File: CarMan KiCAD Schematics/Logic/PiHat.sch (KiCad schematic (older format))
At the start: 15 parts

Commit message: Refactored repo
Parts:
- gave numbers to parts that had none: 15
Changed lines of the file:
@@
 5V
 $Comp
-L Interface_CAN_LIN:MCP2515-xSO U?
+L Interface_CAN_LIN:MCP2515-xSO U8
 U 1 1 5F9A99EE
 P 6750 3100
-F 0 "U?" H 6500 3850 50  0000 C CNN
+F 0 "U8" H 6500 3850 50  0000 C CNN
 F 1 "MCP2515-xSO" H 7200 3850 50  0000 C CNN
 F 2 "Package_SO:SOIC-18W_7.5x11.6mm_P1.27mm" H 6750 2200 50  0001 C CIN
@@
 5V_rtn
 $Comp
-L Connector:Conn_01x02_Male J?
+L Connector:Conn_01x02_Male J7
 U 1 1 5F9AE3B8
 P 2500 1700
-F 0 "J?" V 2562 1744 50  0000 L CNN
+F 0 "J7" V 2562 1744 50  0000 L CNN
 F 1 "Conn_01x02_Male" V 2653 1744 50  0000 L CNN
 F 2 "" H 2500 1700 50  0001 C CNN
@@
 $EndComp
 $Comp
-L Device:R R?
+L Device:R R7
 U 1 1 5F9AF7D2
 P 2500 2050
-F 0 "R?" H 2570 2096 50  0000 L CNN
+F 0 "R7" H 2570 2096 50  0000 L CNN
 F 1 "120" V 2500 2000 50  0000 L CNN
 F 2 "" V 2430 2050 50  0001 C CNN
@@
 	3600 1850 3900 1850
 $Comp
-L Device:C C?
+L Device:C C14
 U 1 1 5F9B08F3
 P 3900 2000
-F 0 "C?" H 4015 2046 50  0000 L CNN
+F 0 "C14" H 4015 2046 50  0000 L CNN
 F 1 "0.1uF" H 4015 1955 50  0000 L CNN
 F 2 "" H 3938 1850 50  0001 C CNN
@@
 	3600 3250 3700 3250
 $Comp
-L Device:R R?
+L Device:R R6
 U 1 1 5F9B1617
 P 2450 3200
-F 0 "R?" H 2520 3246 50  0000 L CNN
+F 0 "R6" H 2520 3246 50  0000 L CNN
 F 1 "100" V 2450 3150 50  0000 L CNN
 F 2 "" V 2380 3200 50  0001 C CNN
@@
 $EndComp
 $Comp
-L Device:C C?
+L Device:C C12
 U 1 1 5F9B20E3
 P 2450 3500
-F 0 "C?" H 2250 3550 50  0000 L CNN
+F 0 "C12" H 2250 3550 50  0000 L CNN
 F 1 "560pF" H 2100 3450 50  0000 L CNN
 F 2 "" H 2488 3350 50  0001 C CNN
@@
 $EndComp
 $Comp
-L Device:R R?
+L Device:R R8
 U 1 1 5F9B2DC0
 P 2750 3200
-F 0 "R?" H 2820 3246 50  0000 L CNN
+F 0 "R8" H 2820 3246 50  0000 L CNN
 F 1 "100" V 2750 3150 50  0000 L CNN
 F 2 "" V 2680 3200 50  0001 C CNN
@@
 $EndComp
 $Comp
-L Device:C C?
+L Device:C C13
 U 1 1 5F9B3945
 P 2750 3500
-F 0 "C?" H 2865 3546 50  0000 L CNN
+F 0 "C13" H 2865 3546 50  0000 L CNN
 F 1 "560pF" H 2865 3455 50  0000 L CNN
 F 2 "" H 2788 3350 50  0001 C CNN
@@
 	4250 2900 4250 3100
 $Comp
-L Device:R R?
+L Device:R R9
 U 1 1 5F9B562B
 P 4250 3250
-F 0 "R?" H 4320 3296 50  0000 L CNN
+F 0 "R9" H 4320 3296 50  0000 L CNN
 F 1 "4k7" V 4250 3200 50  0000 L CNN
 F 2 "" V 4180 3250 50  0001 C CNN
@@
 NoConn ~ 7350 3500
 $Comp
-L Interface_CAN_LIN:MCP2551-I-P U?
+L Interface_CAN_LIN:MCP2551-I-P U7
 U 1 1 5F9A8A6F
 P 3600 2700
-F 0 "U?" H 3300 3050 50  0000 C CNN
+F 0 "U7" H 3300 3050 50  0000 C CNN
 F 1 "MCP2551-I-P" H 4000 3050 50  0000 C CNN
 F 2 "Package_DIP:DIP-8_W7.62mm" H 3600 2200 50  0001 C CIN
@@
 	6750 1850 7050 1850
 $Comp
-L Device:C C?
+L Device:C C15
 U 1 1 5F9BD77C
 P 7050 2000
-F 0 "C?" H 7165 2046 50  0000 L CNN
+F 0 "C15" H 7165 2046 50  0000 L CNN
 F 1 "0.1uF" H 7165 1955 50  0000 L CNN
 F 2 "" H 7088 1850 50  0001 C CNN
@@
 NoConn ~ 6150 3600
 $Comp
-L Device:R R?
+L Device:R R10
 U 1 1 5F9C01C9
 P 5750 3700
-F 0 "R?" V 5850 3700 50  0000 C CNN
+F 0 "R10" V 5850 3700 50  0000 C CNN
 F 1 "4k7" V 5750 3700 50  0000 C CNN
 F 2 "" V 5680 3700 50  0001 C CNN
@@
 PI_SPI_SCLK
 $Comp
-L Device:Crystal Y?
+L Device:Crystal Y1
 U 1 1 5F9C41DC
 P 8150 3350
-F 0 "Y?" V 8104 3481 50  0000 L CNN
+F 0 "Y1" V 8104 3481 50  0000 L CNN
 F 1 "16MHz" V 8195 3481 50  0000 L CNN
 F 2 "" H 8150 3350 50  0001 C CNN
@@
 	7700 3500 8150 3500
 $Comp
-L Device:C C?
+L Device:C C16
 U 1 1 5F9C8133
 P 8750 3200
-F 0 "C?" V 8498 3200 50  0000 C CNN
+F 0 "C16" V 8498 3200 50  0000 C CNN
 F 1 "22pF" V 8589 3200 50  0000 C CNN
 F 2 "" H 8788 3050 50  0001 C CNN
@@
 Connection ~ 8150 3200
 $Comp
-L Device:C C?
+L Device:C C17
 U 1 1 5F9CA3A5
 P 8750 3500
-F 0 "C?" V 9000 3500 50  0000 C CNN
+F 0 "C17" V 9000 3500 50  0000 C CNN
 F 1 "22pF" V 8900 3500 50  0000 C CNN
 F 2 "" H 8788 3350 50  0001 C CNN

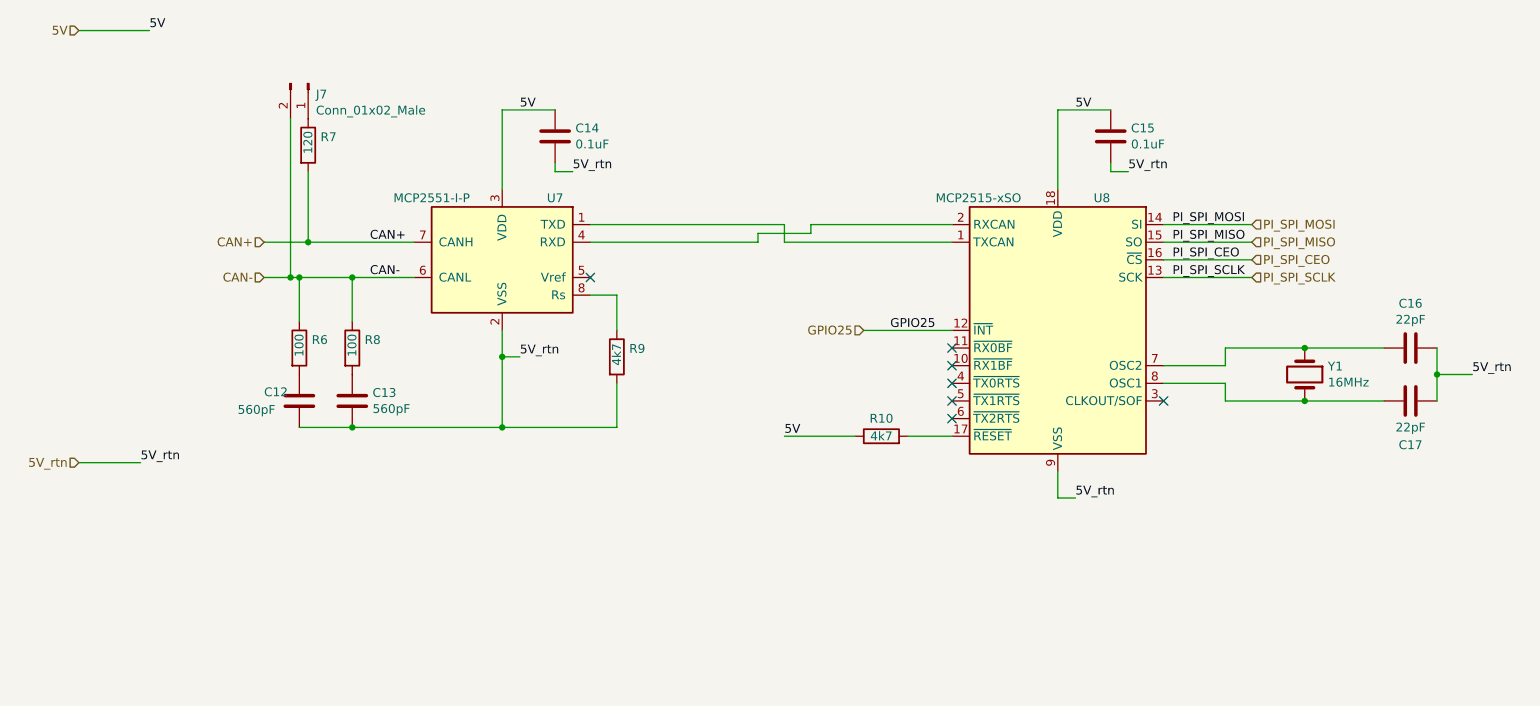
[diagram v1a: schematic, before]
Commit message: Added isolation to CANBUS
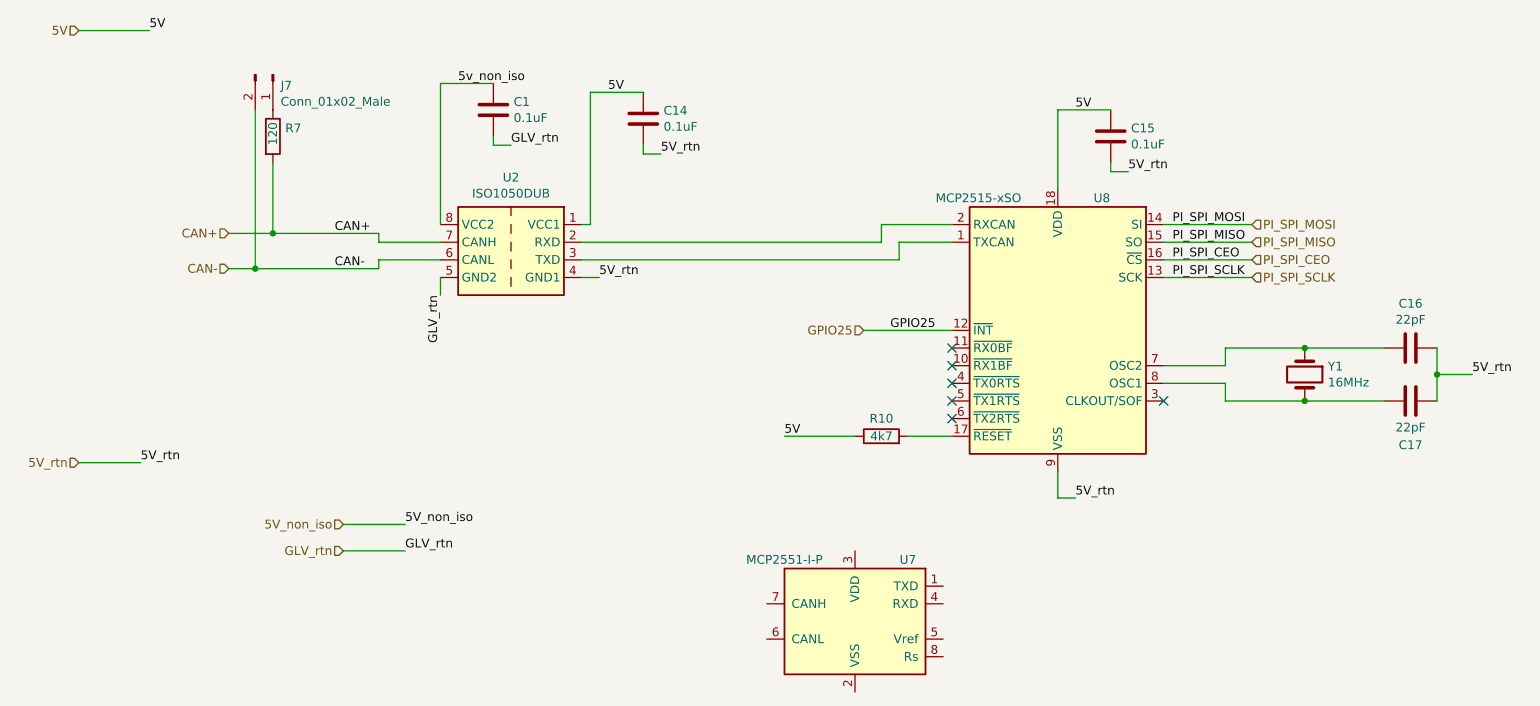
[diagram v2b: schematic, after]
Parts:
- removed C12, C13: 560pF, symbol Device:C
- removed R6, R8: 100, symbol Device:R
- removed R9: 4k7, symbol Device:R
- added C1: 0.1uF, symbol Device:C
- added U2: ISO1050DUB, Package_SO:SOP-8_6.62x9.15mm_P2.54mm, symbol Interface_CAN_LIN:ISO1050DUB
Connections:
- net 5V: now also U2.1 (VCC1); no longer U7.3 (VDD)
- net 5V_rtn: now also U2.4 (GND1); no longer U7.2 (VSS)
- net CAN+: now also U2.7 (CANH); no longer U7.7 (CANH)
- net CAN-: now also U2.6 (CANL); no longer U7.6 (CANL)
- net at U7.1 (TXD): no longer U8.1 (TXCAN)
- net at U7.4 (RXD): no longer U8.2 (RXCAN)
- new net: U2.3 (TXD), U8.1 (TXCAN)
- new net: U2.2 (RXD), U8.2 (RXCAN)
- new net 5v_non_iso: C1.1, U2.8 (VCC2)
- new net GLV_rtn: C1.2, U2.5 (GND2)
- no-connect marks 7 -> 6
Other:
- moved on the sheet: C14, J7, R7, U7
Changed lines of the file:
@@
 Text HLabel 1200 3850 0    50   Input ~ 0
 5V_rtn
-Text HLabel 2250 2800 0    50   Input ~ 0
+Text HLabel 2050 2750 0    50   Input ~ 0
 CAN-
-Text HLabel 2250 2600 0    50   Input ~ 0
+Text HLabel 2050 2550 0    50   Input ~ 0
 CAN+
 Wire Wire Line
-	2250 2600 2500 2600
-Wire Wire Line
-	2250 2800 2400 2800
+	2050 2550 2300 2550
+Wire Wire Line
+	2050 2750 2200 2750
 Wire Wire Line
 	1200 1400 1600 1400
 Wire Wire Line
 	1200 3850 1550 3850
-Text Label 2850 2600 0    50   ~ 0
+Text Label 2650 2550 0    50   ~ 0
 CAN+
-Text Label 2850 2800 0    50   ~ 0
+Text Label 2650 2750 0    50   ~ 0
 CAN-
 Text Label 1600 1400 0    50   ~ 0
@@
 L Connector:Conn_01x02_Male J7
 U 1 1 5F9AE3B8
-P 2500 1700
-F 0 "J7" V 2562 1744 50  0000 L CNN
-F 1 "Conn_01x02_Male" V 2653 1744 50  0000 L CNN
-F 2 "" H 2500 1700 50  0001 C CNN
-F 3 "~" H 2500 1700 50  0001 C CNN
-	1    2500 1700
+P 2300 1650
+F 0 "J7" V 2362 1694 50  0000 L CNN
+F 1 "Conn_01x02_Male" V 2453 1694 50  0000 L CNN
+F 2 "" H 2300 1650 50  0001 C CNN
+F 3 "~" H 2300 1650 50  0001 C CNN
+	1    2300 1650
 	0    1    1    0
 $EndComp
@@
 L Device:R R7
 U 1 1 5F9AF7D2
-P 2500 2050
-F 0 "R7" H 2570 2096 50  0000 L CNN
-F 1 "120" V 2500 2000 50  0000 L CNN
-F 2 "" V 2430 2050 50  0001 C CNN
-F 3 "~" H 2500 2050 50  0001 C CNN
-	1    2500 2050
+P 2300 2000
+F 0 "R7" H 2370 2046 50  0000 L CNN
+F 1 "120" V 2300 1950 50  0000 L CNN
+F 2 "" V 2230 2000 50  0001 C CNN
+F 3 "~" H 2300 2000 50  0001 C CNN
+	1    2300 2000
 	1    0    0    -1
 $EndComp
 Wire Wire Line
-	2500 2200 2500 2600
-Connection ~ 2500 2600
-Wire Wire Line
-	2500 2600 3100 2600
-Wire Wire Line
-	2400 1900 2400 2800
-Connection ~ 2400 2800
-Wire Wire Line
-	2400 2800 2450 2800
-Wire Wire Line
-	3600 2300 3600 1850
-Wire Wire Line
-	3600 1850 3900 1850
+	2300 2150 2300 2550
+Connection ~ 2300 2550
+Wire Wire Line
+	2300 2550 2900 2550
+Wire Wire Line
+	2200 1850 2200 2750
+Connection ~ 2200 2750
+Wire Wire Line
+	4100 1750 4400 1750
 $Comp
 L Device:C C14
 U 1 1 5F9B08F3
-P 3900 2000
-F 0 "C14" H 4015 2046 50  0000 L CNN
-F 1 "0.1uF" H 4015 1955 50  0000 L CNN
-F 2 "" H 3938 1850 50  0001 C CNN
-F 3 "~" H 3900 2000 50  0001 C CNN
-	1    3900 2000
+P 4400 1900
+F 0 "C14" H 4515 1946 50  0000 L CNN
+F 1 "0.1uF" H 4515 1855 50  0000 L CNN
+F 2 "" H 4438 1750 50  0001 C CNN
+F 3 "~" H 4400 1900 50  0001 C CNN
+	1    4400 1900
 	1    0    0    -1
 $EndComp
 Wire Wire Line
-	3900 2150 3900 2200
-Wire Wire Line
-	3900 2200 4000 2200
-Text Label 3700 1850 0    50   ~ 0
+	4400 2050 4400 2100
+Wire Wire Line
+	4400 2100 4500 2100
+Text Label 4200 1750 0    50   ~ 0
 5V
-Text Label 4000 2200 0    50   ~ 0
-5V_rtn
-Text Label 3700 3250 0    50   ~ 0
-5V_rtn
-Wire Wire Line
-	3600 3100 3600 3250
-Wire Wire Line
-	3600 3250 3700 3250
-$Comp
-L Device:R R6
-U 1 1 5F9B1617
-P 2450 3200
-F 0 "R6" H 2520 3246 50  0000 L CNN
-F 1 "100" V 2450 3150 50  0000 L CNN
-F 2 "" V 2380 3200 50  0001 C CNN
-F 3 "~" H 2450 3200 50  0001 C CNN
-	1    2450 3200
-	1    0    0    -1
-$EndComp
-$Comp
-L Device:C C12
-U 1 1 5F9B20E3
-P 2450 3500
-F 0 "C12" H 2250 3550 50  0000 L CNN
-F 1 "560pF" H 2100 3450 50  0000 L CNN
-F 2 "" H 2488 3350 50  0001 C CNN
-F 3 "~" H 2450 3500 50  0001 C CNN
-	1    2450 3500
-	1    0    0    -1
-$EndComp
-$Comp
-L Device:R R8
-U 1 1 5F9B2DC0
-P 2750 3200
-F 0 "R8" H 2820 3246 50  0000 L CNN
-F 1 "100" V 2750 3150 50  0000 L CNN
-F 2 "" V 2680 3200 50  0001 C CNN
-F 3 "~" H 2750 3200 50  0001 C CNN
-	1    2750 3200
-	1    0    0    -1
-$EndComp
-$Comp
-L Device:C C13
-U 1 1 5F9B3945
-P 2750 3500
-F 0 "C13" H 2865 3546 50  0000 L CNN
-F 1 "560pF" H 2865 3455 50  0000 L CNN
-F 2 "" H 2788 3350 50  0001 C CNN
-F 3 "~" H 2750 3500 50  0001 C CNN
-	1    2750 3500
-	1    0    0    -1
-$EndComp
-Wire Wire Line
-	3600 3250 3600 3650
-Wire Wire Line
-	3600 3650 2750 3650
-Connection ~ 3600 3250
-Wire Wire Line
-	2450 3650 2750 3650
-Connection ~ 2750 3650
-Wire Wire Line
-	2750 3050 2750 2800
-Connection ~ 2750 2800
-Wire Wire Line
-	2750 2800 3100 2800
-Wire Wire Line
-	2450 3050 2450 2800
-Connection ~ 2450 2800
-Wire Wire Line
-	2450 2800 2750 2800
-Wire Wire Line
-	4100 2900 4250 2900
-Wire Wire Line
-	4250 2900 4250 3100
-$Comp
-L Device:R R9
-U 1 1 5F9B562B
-P 4250 3250
-F 0 "R9" H 4320 3296 50  0000 L CNN
-F 1 "4k7" V 4250 3200 50  0000 L CNN
-F 2 "" V 4180 3250 50  0001 C CNN
-F 3 "~" H 4250 3250 50  0001 C CNN
-	1    4250 3250
-	1    0    0    -1
-$EndComp
-Wire Wire Line
-	4250 3400 4250 3650
-Wire Wire Line
-	4250 3650 3600 3650
-Connection ~ 3600 3650
-Wire Wire Line
-	4100 2500 5200 2500
-Wire Wire Line
-	5200 2500 5200 2600
-Wire Wire Line
-	5200 2600 6150 2600
-Wire Wire Line
-	4100 2600 5050 2600
-Wire Wire Line
-	5050 2600 5050 2550
-Wire Wire Line
-	5050 2550 5350 2550
-Wire Wire Line
-	5350 2550 5350 2500
-Wire Wire Line
-	5350 2500 6150 2500
-NoConn ~ 4100 2800
+Text Label 4500 2100 0    50   ~ 0
+5V_rtn
+Text Label 4150 2800 0    50   ~ 0
+5V_rtn
+Wire Wire Line
+	4050 2800 4150 2800
 NoConn ~ 7350 3500
 $Comp
 L Interface_CAN_LIN:MCP2551-I-P U7
 U 1 1 5F9A8A6F
-P 3600 2700
-F 0 "U7" H 3300 3050 50  0000 C CNN
-F 1 "MCP2551-I-P" H 4000 3050 50  0000 C CNN
-F 2 "Package_DIP:DIP-8_W7.62mm" H 3600 2200 50  0001 C CIN
-F 3 "http://ww1.microchip.com/downloads/en/devicedoc/21667d.pdf" H 3600 2700 50  0001 C CNN
-	1    3600 2700
+P 5600 4750
+F 0 "U7" H 5300 5100 50  0000 C CNN
+F 1 "MCP2551-I-P" H 6000 5100 50  0000 C CNN
+F 2 "Package_DIP:DIP-8_W7.62mm" H 5600 4250 50  0001 C CIN
+F 3 "http://ww1.microchip.com/downloads/en/devicedoc/21667d.pdf" H 5600 4750 50  0001 C CNN
+	1    5600 4750
 	-1   0    0    -1
 $EndComp
@@
 Text HLabel 7850 2800 2    50   Input ~ 0
 PI_SPI_SCLK
+$Comp
+L Interface_CAN_LIN:ISO1050DUB U2
+U 1 1 5FAD2713
+P 3650 2600
+F 0 "U2" H 3650 2967 50  0000 C CNN
+F 1 "ISO1050DUB" H 3650 2876 50  0000 C CNN
+F 2 "Package_SO:SOP-8_6.62x9.15mm_P2.54mm" H 3650 2250 50  0001 C CIN
+F 3 "http://www.ti.com/lit/ds/symlink/iso1050.pdf" H 3650 2550 50  0001 C CNN
+	1    3650 2600
+	-1   0    0    -1
+$EndComp
+Wire Wire Line
+	4100 2500 4050 2500
+Wire Wire Line
+	4100 1750 4100 2500
+Wire Wire Line
+	4050 2700 5850 2700
+Wire Wire Line
+	5850 2700 5850 2600
+Wire Wire Line
+	5850 2600 6150 2600
+Wire Wire Line
+	4050 2600 5750 2600
+Wire Wire Line
+	5750 2600 5750 2500
+Wire Wire Line
+	5750 2500 6150 2500
+Wire Wire Line
+	3250 1700 3550 1700
+$Comp
+L Device:C C1
+U 1 1 5FADAB07
+P 3550 1850
+F 0 "C1" H 3665 1896 50  0000 L CNN
+F 1 "0.1uF" H 3665 1805 50  0000 L CNN
+F 2 "" H 3588 1700 50  0001 C CNN
+F 3 "~" H 3550 1850 50  0001 C CNN
+	1    3550 1850
+	1    0    0    -1
+$EndComp
+Wire Wire Line
+	3550 2000 3550 2050
+Wire Wire Line
+	3550 2050 3650 2050
+Text Label 3350 1700 0    50   ~ 0
+5v_non_iso
+Text Label 3650 2050 0    50   ~ 0
+GLV_rtn
+Text HLabel 2700 4200 0    50   Input ~ 0
+5V_non_iso
+Wire Wire Line
+	2700 4200 3050 4200
+Text Label 3050 4200 0    50   ~ 0
+5V_non_iso
+Wire Wire Line
+	2200 2750 2900 2750
+Wire Wire Line
+	3250 2600 2900 2600
+Wire Wire Line
+	2900 2600 2900 2550
+Wire Wire Line
+	2900 2750 2900 2700
+Wire Wire Line
+	2900 2700 3250 2700
+Wire Wire Line
+	3250 1700 3250 2500
+Text HLabel 2700 4350 0    50   Input ~ 0
+GLV_rtn
+Wire Wire Line
+	2700 4350 3050 4350
+Text Label 3050 4350 0    50   ~ 0
+GLV_rtn
+Text Label 3250 2900 3    50   ~ 0
+GLV_rtn
+Wire Wire Line
+	3250 2800 3250 2900
 $EndSCHEMATC

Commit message: Fixed Logic Board
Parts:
- removed U7: MCP2551-I-P, Package_DIP:DIP-8_W7.62mm, symbol Interface_CAN_LIN:MCP2551-I-P
- C1, C14, C15, C16, C17: symbol Device:C -> Logic-rescue:C-Device-Logic-rescue
- J7: symbol Connector:Conn_01x02_Male -> Logic-rescue:Conn_01x02_Male-Connector-Logic-rescue
- R10, R7: symbol Device:R -> Logic-rescue:R-Device-Logic-rescue
- U2: symbol Interface_CAN_LIN:ISO1050DUB -> Logic-rescue:ISO1050DUB-Interface_CAN_LIN-Logic-rescue
- U8: symbol Interface_CAN_LIN:MCP2515-xSO -> Logic-rescue:MCP2515-xSO-Interface_CAN_LIN-Logic-rescue
- Y1: symbol Device:Crystal -> Logic-rescue:Crystal-Device-Logic-rescue
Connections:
- net 5v_non_iso is gone; now on net 5V_non_iso: C1.1, U2.8 (VCC2)
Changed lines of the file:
@@
 5V
 $Comp
-L Interface_CAN_LIN:MCP2515-xSO U8
+L Logic-rescue:MCP2515-xSO-Interface_CAN_LIN-Logic-rescue U8
 U 1 1 5F9A99EE
 P 6750 3100
@@
 5V_rtn
 $Comp
-L Connector:Conn_01x02_Male J7
+L Logic-rescue:Conn_01x02_Male-Connector-Logic-rescue J7
 U 1 1 5F9AE3B8
 P 2300 1650
-F 0 "J7" V 2362 1694 50  0000 L CNN
+AR Path="/5F9AE3B8" Ref="J7"  Part="1"
+AR Path="/5F9A7CF0/5F9AE3B8" Ref="J9"  Part="1"
+F 0 "J9" V 2362 1694 50  0000 L CNN
 F 1 "Conn_01x02_Male" V 2453 1694 50  0000 L CNN
 F 2 "" H 2300 1650 50  0001 C CNN
@@
 $EndComp
 $Comp
-L Device:R R7
+L Logic-rescue:R-Device-Logic-rescue R7
 U 1 1 5F9AF7D2
 P 2300 2000
+AR Path="/5F9AF7D2" Ref="R7"  Part="1"
+AR Path="/5F9A7CF0/5F9AF7D2" Ref="R7"  Part="1"
 F 0 "R7" H 2370 2046 50  0000 L CNN
 F 1 "120" V 2300 1950 50  0000 L CNN
@@
 	4100 1750 4400 1750
 $Comp
-L Device:C C14
+L Logic-rescue:C-Device-Logic-rescue C14
 U 1 1 5F9B08F3
 P 4400 1900
+AR Path="/5F9B08F3" Ref="C14"  Part="1"
+AR Path="/5F9A7CF0/5F9B08F3" Ref="C14"  Part="1"
 F 0 "C14" H 4515 1946 50  0000 L CNN
 F 1 "0.1uF" H 4515 1855 50  0000 L CNN
@@
 	4050 2800 4150 2800
 NoConn ~ 7350 3500
-$Comp
-L Interface_CAN_LIN:MCP2551-I-P U7
-U 1 1 5F9A8A6F
-P 5600 4750
-F 0 "U7" H 5300 5100 50  0000 C CNN
-F 1 "MCP2551-I-P" H 6000 5100 50  0000 C CNN
-F 2 "Package_DIP:DIP-8_W7.62mm" H 5600 4250 50  0001 C CIN
-F 3 "http://ww1.microchip.com/downloads/en/devicedoc/21667d.pdf" H 5600 4750 50  0001 C CNN
-	1    5600 4750
-	-1   0    0    -1
-$EndComp
 Text Label 6850 4050 0    50   ~ 0
 5V_rtn
@@
 	6750 1850 7050 1850
 $Comp
-L Device:C C15
+L Logic-rescue:C-Device-Logic-rescue C15
 U 1 1 5F9BD77C
 P 7050 2000
+AR Path="/5F9BD77C" Ref="C15"  Part="1"
+AR Path="/5F9A7CF0/5F9BD77C" Ref="C15"  Part="1"
 F 0 "C15" H 7165 2046 50  0000 L CNN
 F 1 "0.1uF" H 7165 1955 50  0000 L CNN
@@
 NoConn ~ 6150 3600
 $Comp
-L Device:R R10
+L Logic-rescue:R-Device-Logic-rescue R10
 U 1 1 5F9C01C9
 P 5750 3700
+AR Path="/5F9C01C9" Ref="R10"  Part="1"
+AR Path="/5F9A7CF0/5F9C01C9" Ref="R10"  Part="1"
 F 0 "R10" V 5850 3700 50  0000 C CNN
 F 1 "4k7" V 5750 3700 50  0000 C CNN
@@
 PI_SPI_SCLK
 $Comp
-L Device:Crystal Y1
+L Logic-rescue:Crystal-Device-Logic-rescue Y1
 U 1 1 5F9C41DC
 P 8150 3350
@@
 	7700 3500 8150 3500
 $Comp
-L Device:C C16
+L Logic-rescue:C-Device-Logic-rescue C16
 U 1 1 5F9C8133
 P 8750 3200
+AR Path="/5F9C8133" Ref="C16"  Part="1"
+AR Path="/5F9A7CF0/5F9C8133" Ref="C16"  Part="1"
 F 0 "C16" V 8498 3200 50  0000 C CNN
 F 1 "22pF" V 8589 3200 50  0000 C CNN
@@
 Connection ~ 8150 3200
 $Comp
-L Device:C C17
+L Logic-rescue:C-Device-Logic-rescue C17
 U 1 1 5F9CA3A5
 P 8750 3500
+AR Path="/5F9CA3A5" Ref="C17"  Part="1"
+AR Path="/5F9A7CF0/5F9CA3A5" Ref="C17"  Part="1"
 F 0 "C17" V 9000 3500 50  0000 C CNN
 F 1 "22pF" V 8900 3500 50  0000 C CNN
@@
 PI_SPI_SCLK
 $Comp
-L Interface_CAN_LIN:ISO1050DUB U2
+L Logic-rescue:ISO1050DUB-Interface_CAN_LIN-Logic-rescue U2
 U 1 1 5FAD2713
 P 3650 2600
@@
 	3250 1700 3550 1700
 $Comp
-L Device:C C1
+L Logic-rescue:C-Device-Logic-rescue C1
 U 1 1 5FADAB07
 P 3550 1850
+AR Path="/5FADAB07" Ref="C1"  Part="1"
+AR Path="/5F9A7CF0/5FADAB07" Ref="C1"  Part="1"
 F 0 "C1" H 3665 1896 50  0000 L CNN
 F 1 "0.1uF" H 3665 1805 50  0000 L CNN
@@
 	3550 2050 3650 2050
 Text Label 3350 1700 0    50   ~ 0
-5v_non_iso
+5V_non_iso
 Text Label 3650 2050 0    50   ~ 0
 GLV_rtn

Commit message: Logic Footprints in General Library, Added Logic LEDs
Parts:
- C1, C14, C15, C16, C17: footprint (none) -> Capacitor_SMD:C_0805_2012Metric_Pad1.15x1.40mm_HandSolder
- R10, R7: footprint (none) -> Resistor_SMD:R_0815_2038Metric_Pad1.53x4.00mm_HandSolder
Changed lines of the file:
@@
 F 0 "R7" H 2370 2046 50  0000 L CNN
 F 1 "120" V 2300 1950 50  0000 L CNN
-F 2 "" V 2230 2000 50  0001 C CNN
+F 2 "Resistor_SMD:R_0815_2038Metric_Pad1.53x4.00mm_HandSolder" V 2230 2000 50  0001 C CNN
 F 3 "~" H 2300 2000 50  0001 C CNN
 	1    2300 2000
@@
 F 0 "C14" H 4515 1946 50  0000 L CNN
 F 1 "0.1uF" H 4515 1855 50  0000 L CNN
-F 2 "" H 4438 1750 50  0001 C CNN
+F 2 "Capacitor_SMD:C_0805_2012Metric_Pad1.15x1.40mm_HandSolder" H 4438 1750 50  0001 C CNN
 F 3 "~" H 4400 1900 50  0001 C CNN
 	1    4400 1900
@@
 F 0 "C15" H 7165 2046 50  0000 L CNN
 F 1 "0.1uF" H 7165 1955 50  0000 L CNN
-F 2 "" H 7088 1850 50  0001 C CNN
+F 2 "Capacitor_SMD:C_0805_2012Metric_Pad1.15x1.40mm_HandSolder" H 7088 1850 50  0001 C CNN
 F 3 "~" H 7050 2000 50  0001 C CNN
 	1    7050 2000
@@
 F 0 "R10" V 5850 3700 50  0000 C CNN
 F 1 "4k7" V 5750 3700 50  0000 C CNN
-F 2 "" V 5680 3700 50  0001 C CNN
+F 2 "Resistor_SMD:R_0815_2038Metric_Pad1.53x4.00mm_HandSolder" V 5680 3700 50  0001 C CNN
 F 3 "~" H 5750 3700 50  0001 C CNN
 	1    5750 3700
@@
 F 0 "C16" V 8498 3200 50  0000 C CNN
 F 1 "22pF" V 8589 3200 50  0000 C CNN
-F 2 "" H 8788 3050 50  0001 C CNN
+F 2 "Capacitor_SMD:C_0805_2012Metric_Pad1.15x1.40mm_HandSolder" H 8788 3050 50  0001 C CNN
 F 3 "~" H 8750 3200 50  0001 C CNN
 	1    8750 3200
@@
 F 0 "C17" V 9000 3500 50  0000 C CNN
 F 1 "22pF" V 8900 3500 50  0000 C CNN
-F 2 "" H 8788 3350 50  0001 C CNN
+F 2 "Capacitor_SMD:C_0805_2012Metric_Pad1.15x1.40mm_HandSolder" H 8788 3350 50  0001 C CNN
 F 3 "~" H 8750 3500 50  0001 C CNN
 	1    8750 3500
@@
 F 0 "C1" H 3665 1896 50  0000 L CNN
 F 1 "0.1uF" H 3665 1805 50  0000 L CNN
-F 2 "" H 3588 1700 50  0001 C CNN
+F 2 "Capacitor_SMD:C_0805_2012Metric_Pad1.15x1.40mm_HandSolder" H 3588 1700 50  0001 C CNN
 F 3 "~" H 3550 1850 50  0001 C CNN
 	1    3550 1850
